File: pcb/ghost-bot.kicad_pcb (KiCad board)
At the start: 2 copper layers, 111 x 60 mm, 37 parts, among them J1 Conn_01x03_Pin, J2 Conn_01x03_Pin, J3 Conn_01x04_Pin, J4 Conn_01x02_Pin, SW1 SW_Push, SW2 SW_Push, SW3 SW_SPDT

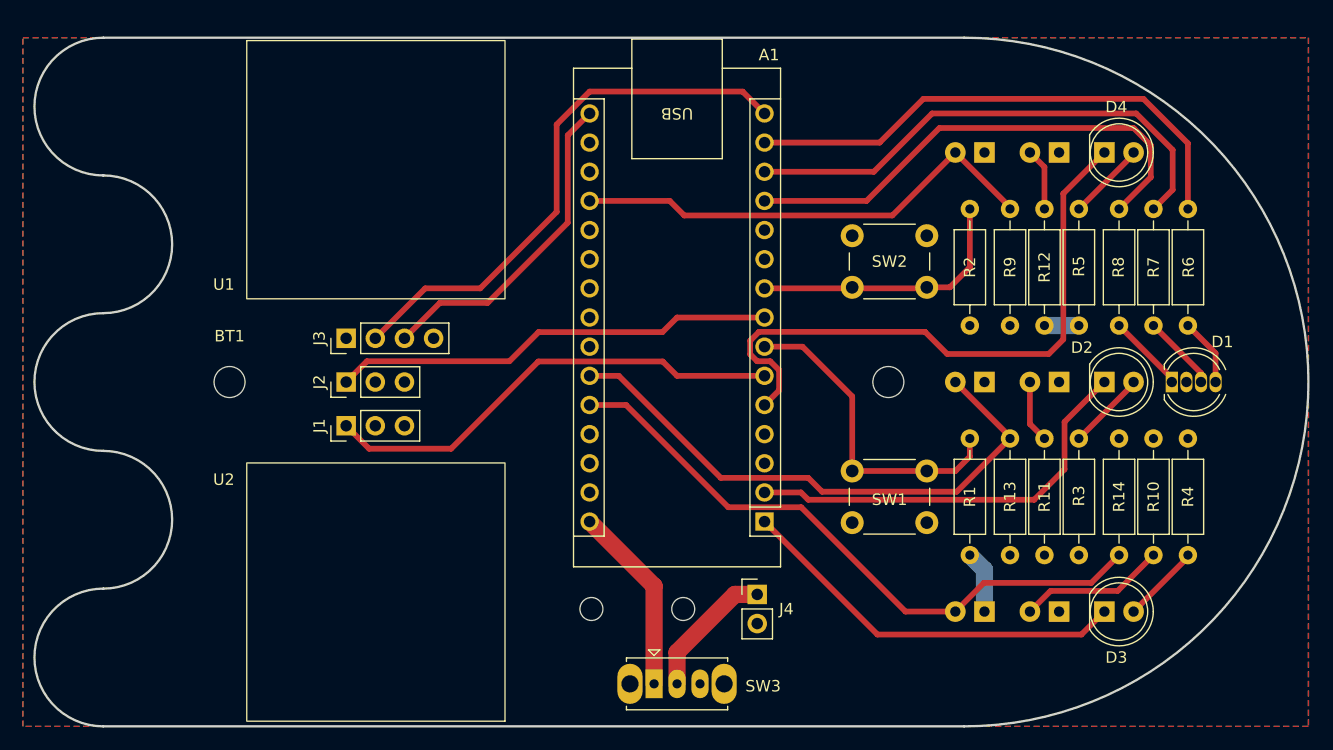
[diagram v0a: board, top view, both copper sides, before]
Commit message: Change +5V from pour to route
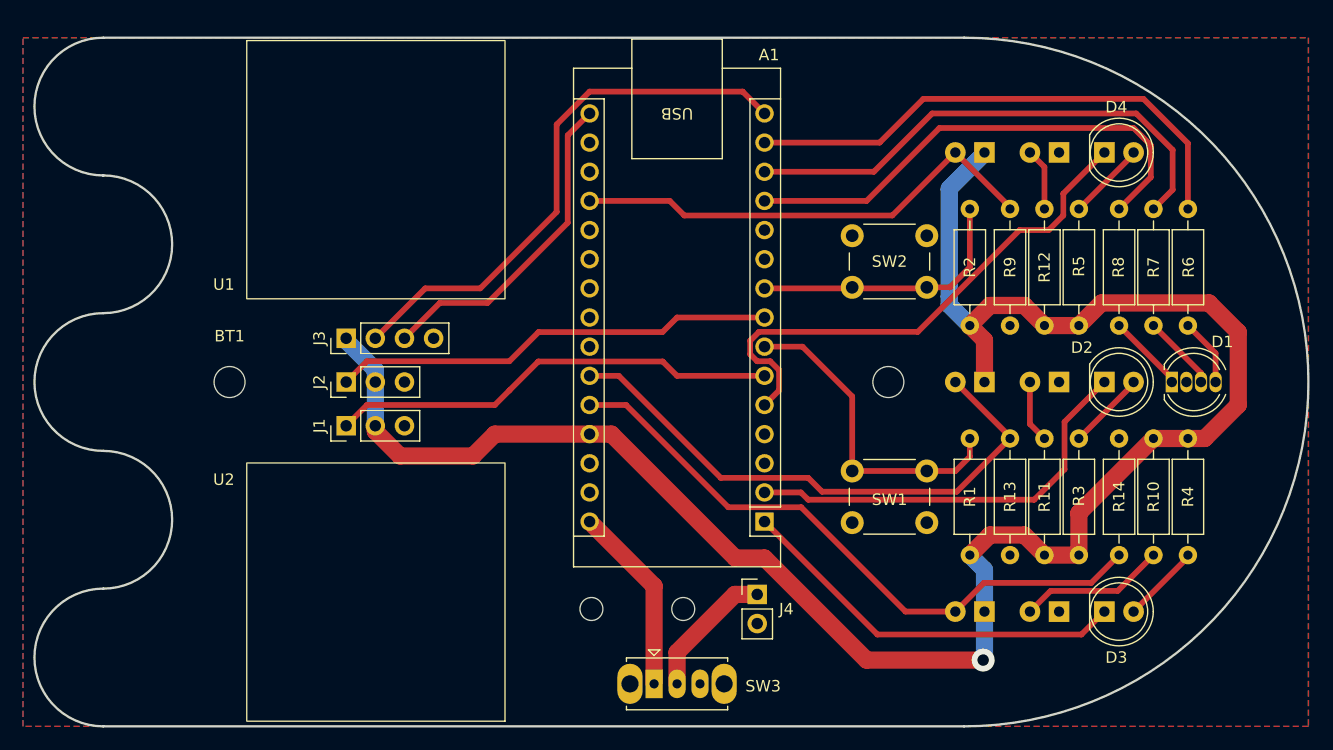
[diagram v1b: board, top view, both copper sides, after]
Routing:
- net +5V: track 8.45 -> 169.7 mm, vias 0 -> 1
- net /LED2: track 54.5 -> 46.6 mm
- net /SERVO0: track 40.9 -> 39.3 mm
- added copper zone on F.Cu, net GND
- removed copper zone on F.Cu, net +5V

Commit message: Update power switch
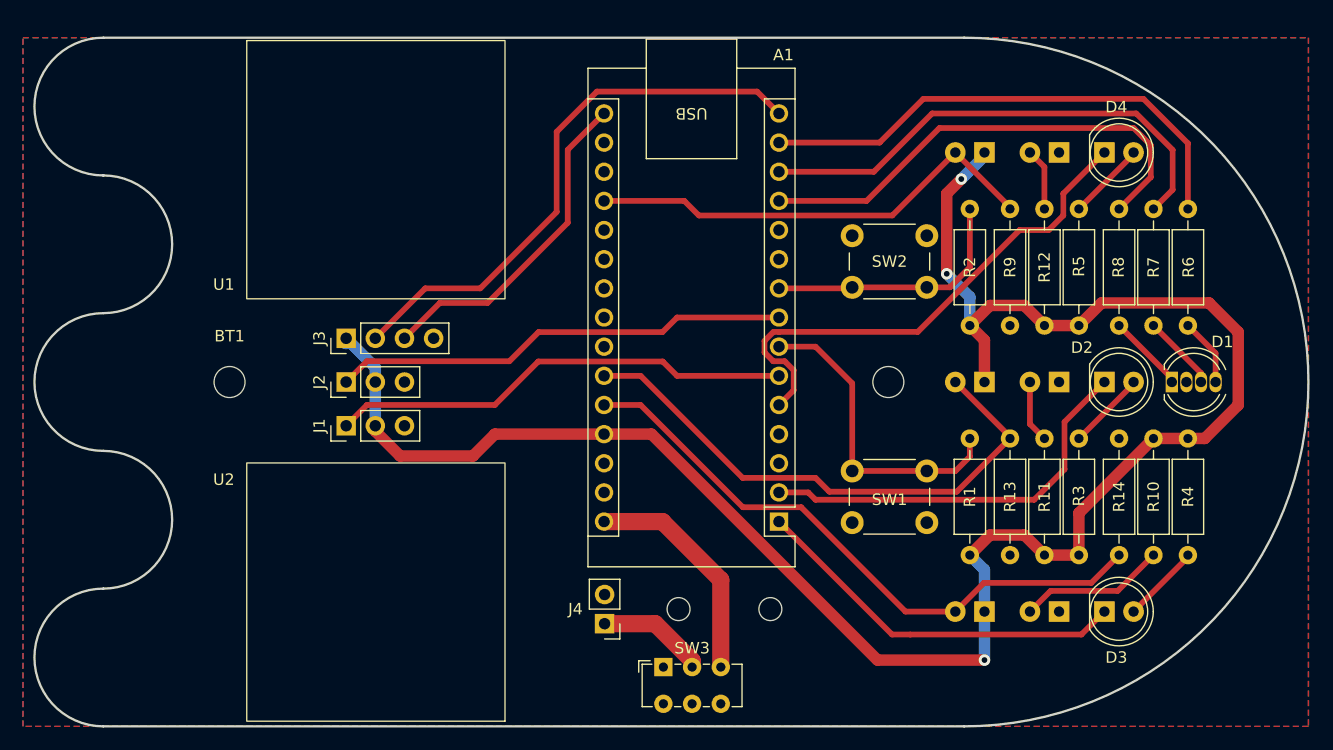
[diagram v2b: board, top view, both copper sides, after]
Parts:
- SW3: value SW_SPDT -> Switch; footprint Button_Switch_THT:SW_Slide_SPDT_Straight_CK_OS102011MS2Q -> Button_Switch_THT:SW_E-Switch_EG1271_SPDT
- moved REF** 15.6 mm to (165.6, 133.8), turned to 180 degrees
- moved J4 13.5 mm to (151.2, 135.1), turned to 180 degrees
- moved SW3 1.67 mm to (156.3, 138.8)
- moved A1 1.26 mm to (166.4, 126.2)
- moved REF** 0.41 mm to (157.6, 133.8), turned to 180 degrees
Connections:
- SW3 pad 1: +BATT_SW -> unconnected-(SW3-C-Pad1)
- SW3 pad 3: unconnected-(SW3-C-Pad3) -> +BATT_SW
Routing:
- net +BATT_SW: track 16.5 -> 19.9 mm
- net +BATT: track 11.8 -> 9.52 mm
- net /LED2: track 46.6 -> 45.3 mm
- net /LED0: track 36.5 -> 35.3 mm
- net /LED1: track 34.5 -> 33.3 mm
- net /SERVO1: track 38.8 -> 40.0 mm
- net /SERVO0: track 39.3 -> 40.5 mm
- net /RGB_R: track 45.8 -> 44.5 mm
- net /RGB_G: track 44.8 -> 43.6 mm
- net /RGB_B: track 43.6 -> 42.3 mm
- net /PD0: track 41.6 -> 40.3 mm
- net /PD2: track 55.6 -> 54.4 mm
- net /PD1: track 49.6 -> 48.4 mm
- net /PUSH_BTN1: track 23.7 -> 22.6 mm
- net /TRIG: track 48.1 -> 49.0 mm
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
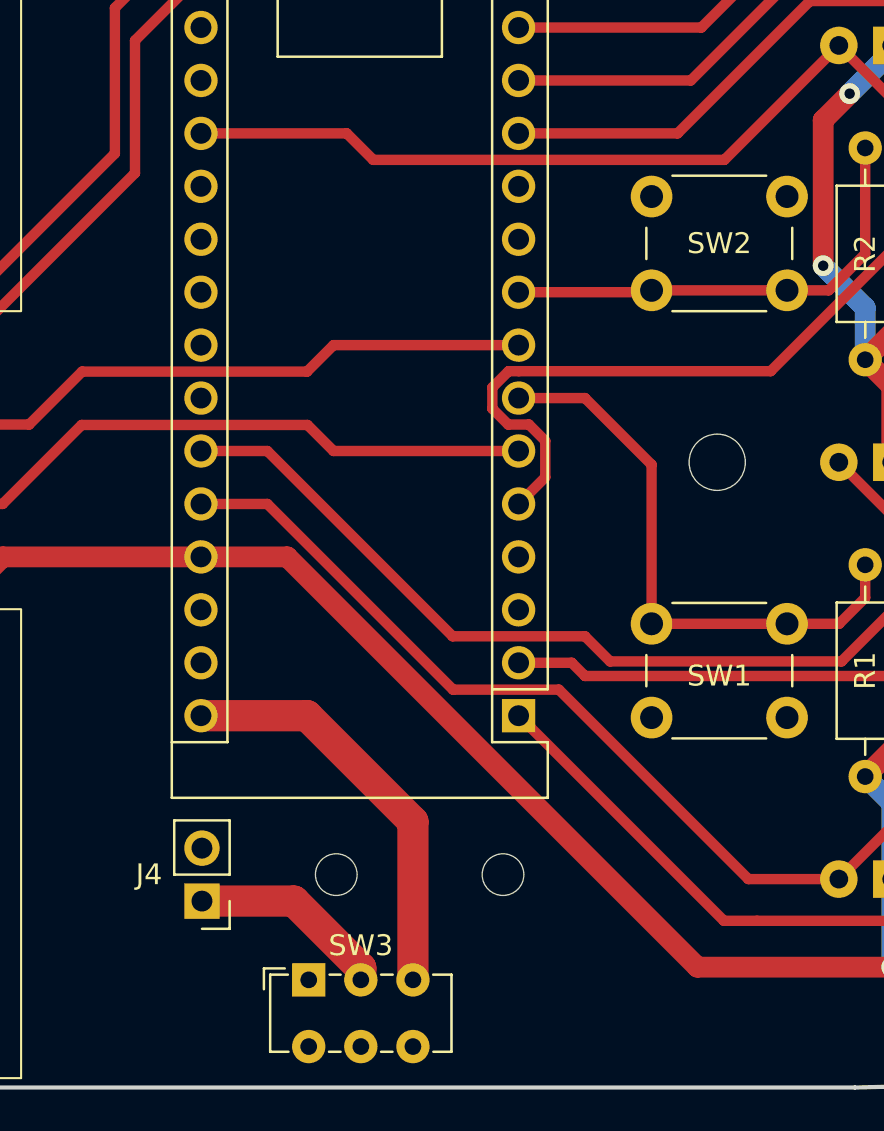
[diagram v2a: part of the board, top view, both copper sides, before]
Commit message: Add version number and blank space for name
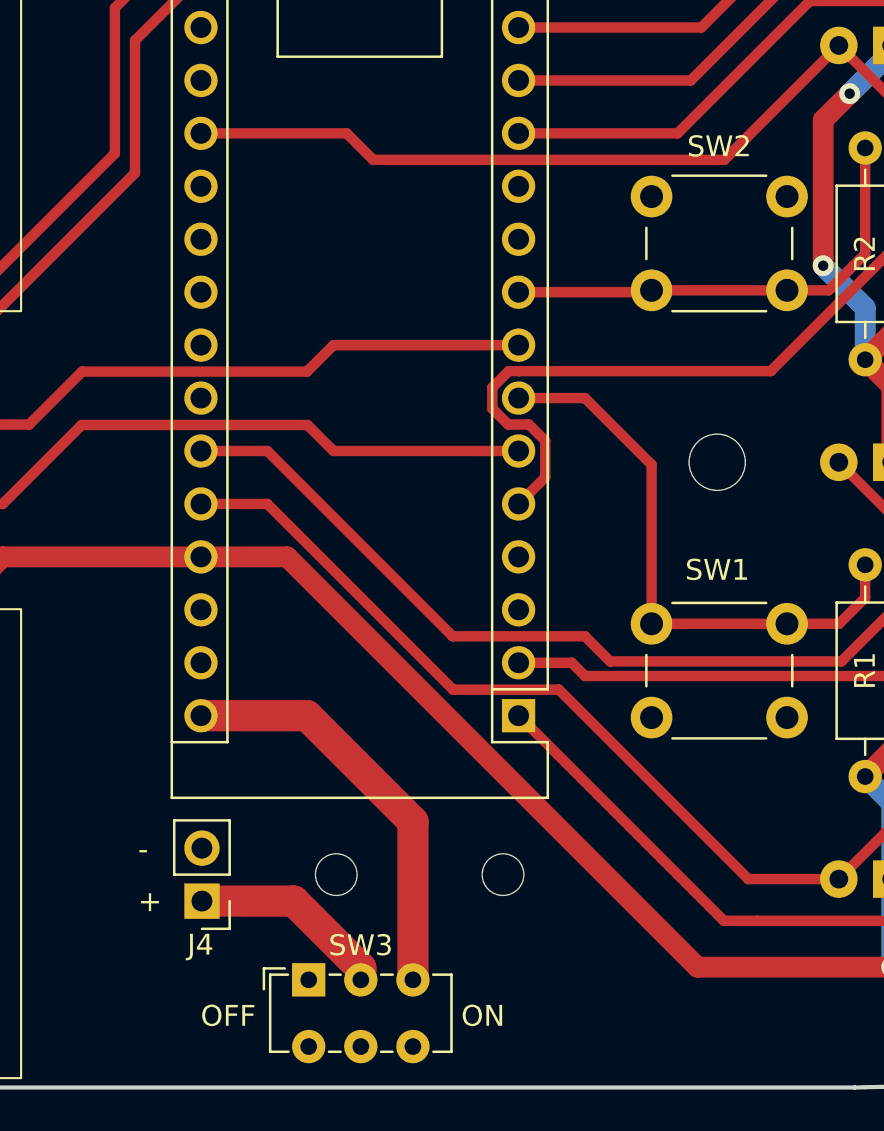
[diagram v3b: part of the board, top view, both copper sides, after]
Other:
- board text added: "+"
- board text added: "-"
- board text added: "GHOST-BOT V0.1 0424 CK"
- board text added: "OFF"
- board text added: "ON"
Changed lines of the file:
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@@
 		(pad_to_mask_clearance 0)
 		(allow_soldermask_bridges_in_footprints no)
-		(grid_origin 165.11 126.16)
+		(grid_origin 131.185 117.81)
 		(pcbplotparams
 			(layerselection 0x00010fc_ffffffff)
@@
 		(tags "Through hole pin header THT 1x02 2.54mm single row")
 		(property "Reference" "J4"
-			(at 2.54 1.275 180)
+			(at 0.067143 -2.105001 180)
 			(layer "F.SilkS")
 			(effects
@@
 		(tags "tact sw push 6mm")
 		(property "Reference" "SW1"
-			(at 3.25 2 180)
+			(at 3.345003 7.075 180)
 			(layer "F.SilkS")
 			(effects
@@
 		(tags "tact sw push 6mm")
 		(property "Reference" "SW2"
-			(at 3.25 2.25 360)
+			(at 3.25 -2.395 360)
 			(layer "F.SilkS")
 			(effects
@@
 		)
 	)
+	(gr_rect
+		(start 115.685 120.06)
+		(end 148.185 128.56)
+		(stroke
+			(width 0.1)
+			(type solid)
+		)
+		(fill solid)
+		(layer "B.SilkS")
+	)
 	(gr_line
 		(start 182.500003 144)
@@
 		(layer "Edge.Cuts")
 	)
+	(gr_text "GHOST-BOT\nV0.1 0424 CK"
+		(at 148.185 107.81 0)
+		(layer "B.SilkS" knockout)
+		(effects
+			(font
+				(size 3 3)
+				(thickness 0.3)
+			)
+			(justify left bottom mirror)
+		)
+	)
+	(gr_text "        \n        "
+		(at 140.11 141.66 0)
+		(layer "B.SilkS" knockout)
+		(effects
+			(font
+				(size 2 2)
+				(thickness 0.2)
+			)
+			(justify left bottom mirror)
+		)
+	)
+	(gr_text "OFF"
+		(at 151.11 141.16 0)
+		(layer "F.SilkS")
+		(effects
+			(font
+				(size 1 1)
+				(thickness 0.1)
+			)
+			(justify left bottom)
+		)
+	)
+	(gr_text "ON"
+		(at 163.61 141.16 0)
+		(layer "F.SilkS")
+		(effects
+			(font
+				(size 1 1)
+				(thickness 0.1)
+			)
+			(justify left bottom)
+		)
+	)
+	(gr_text "-"
+		(at 148.11 133.16 0)
+		(layer "F.SilkS")
+		(effects
+			(font
+				(size 1 1)
+				(thickness 0.1)
+			)
+			(justify left bottom)
+		)
+	)
+	(gr_text "+"
+		(at 148.11 135.66 0)
+		(layer "F.SilkS")
+		(effects
+			(font
+				(size 1 1)
+				(thickness 0.1)
+			)
+			(justify left bottom)
+		)
+	)
 	(segment
 		(start 186.500003 98.765)
@@
 		)
 	)
-	(group ""
-		(members "04ff03a6-6a82-412c-b951-cb5a4e1fd252" "235906f6-29fc-4983-abad-0b41bc71924c"
-			"b5c01504-4c51-43e4-9161-fa676d6fda77"
-		)
-	)

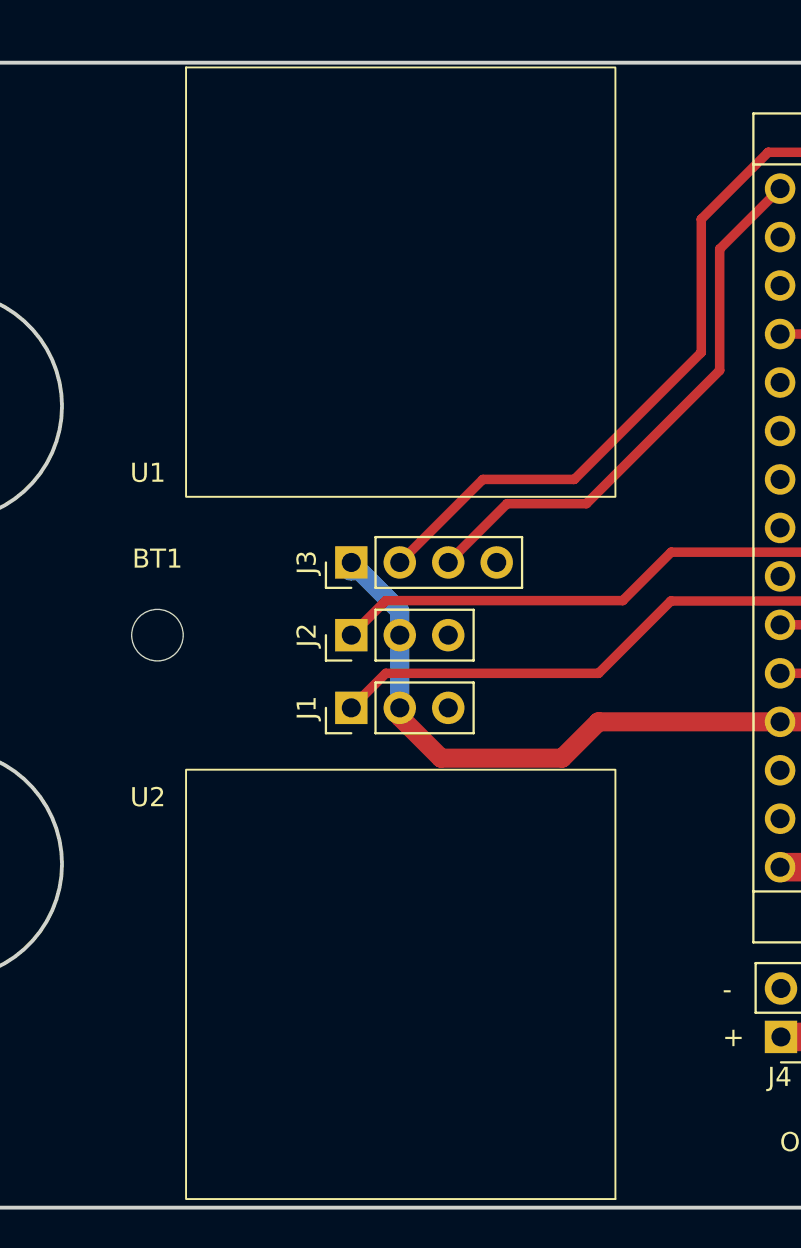
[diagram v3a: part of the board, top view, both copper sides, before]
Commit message: Fix servo 3d model, add battery holder 3d model
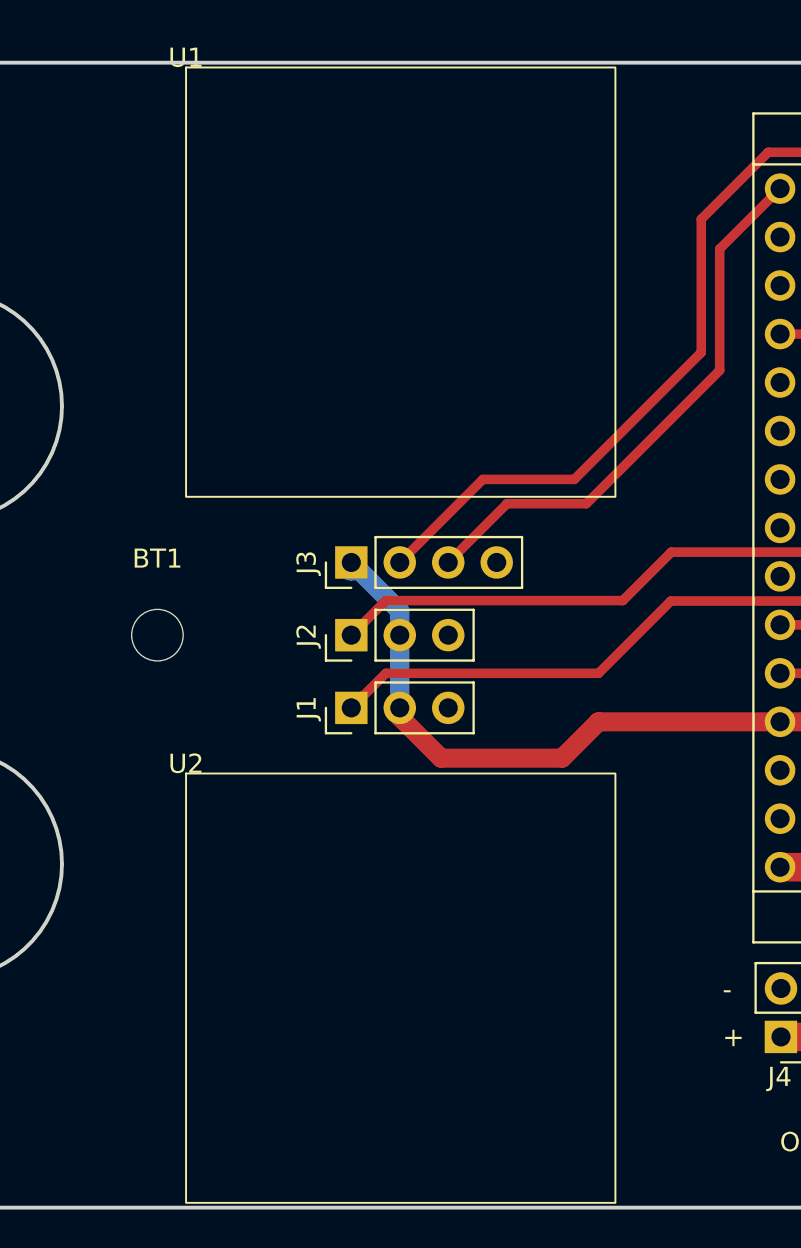
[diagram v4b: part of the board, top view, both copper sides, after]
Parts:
- U1: footprint ghost-bot-footprints:SG90 Mount -> ghost-bot-footprints:SG90 Mount Left
- U2: footprint ghost-bot-footprints:SG90 Mount -> ghost-bot-footprints:SG90 Mount Right
- moved U2 31.7 mm to (120.0, 121.2), turned to 0 degrees
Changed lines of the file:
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@@
 		)
 	)
-	(footprint "ghost-bot-footprints:SG90 Mount"
+	(footprint "ghost-bot-footprints:SG90 Mount Left"
 		(layer "F.Cu")
 		(at 120 84.25)
 		(property "Reference" "U1"
-			(at -1.999997 21.25 0)
+			(at 0 -0.5 0)
 			(unlocked yes)
 			(layer "F.SilkS")
@@
 			)
 		)
-		(property "Footprint" "ghost-bot-footprints:SG90 Mount"
+		(property "Footprint" "ghost-bot-footprints:SG90 Mount Left"
 			(at 0 0 0)
 			(unlocked yes)
@@
 			)
 		)
-		(sheetname "Root")
-		(sheetfile "ghost-bot.kicad_sch")
 		(attr through_hole)
 		(fp_circle
@@
 		)
 		(group ""
-			(members "477627c3-0ea7-40b4-8d42-3f0d67e40fb8" "54bcdb0e-7c43-4856-8c80-bbe86b502977"
-				"5983bcc4-ed36-4caf-9558-bb0dae69b7ae" "8df0314b-b93d-4c92-ba53-34634ea4101a"
-				"ac0160a3-3629-4786-8965-1265075b70f3" "bec5e667-489f-4c43-b3b2-1797f995ca7c"
-				"d24b03ea-7639-4392-9dd7-51629ad52e89" "d7f80189-96fb-43f1-8ea7-0dccd5c6819d"
-				"db8f25e3-8522-4877-baae-065b9b1cb244" "ef4a4cf2-f2c1-4e7a-9d7d-72907f004f8e"
+			(members "065eebc5-e58f-4e5b-9ba1-1c761c134878" "2c3f43af-45b5-4842-b803-4c5029c35410"
+				"3bd75768-710e-4287-b6c3-907f92769104" "56f2f07b-8d62-44bc-bd64-2dcf287d6864"
+				"701e2a11-0f14-494c-988a-4f912dfa61e6" "aa18958b-b5a4-417a-be25-1ae46ee51011"
+				"ca628f01-edbf-4ea8-ad5c-528ef7bb0ef0" "dc04df5b-5c4c-423c-94cf-c9e431fd34a8"
+				"e07d17e8-bc87-48b7-bbab-782ed894ede9" "e5fc3e63-8c5c-41db-b08d-42a8e39c4b29"
 			)
 		)
 		(group ""
-			(members "89dbb5f2-834d-4435-8ff6-2a0a1a8e5e7e" "8ea8d284-649a-4601-8775-b0ddb1f1a850"
-				"c0ae5fb2-2f40-476a-8581-44509fb10b3a"
+			(members "42162b86-009d-4845-8768-e036fcf516e4" "813d3f72-5694-440b-8c18-e3150fbfc66d"
+				"d4edf60a-675a-45d9-8a4b-d10af0728610"
+			)
+		)
+		(model "C:/CAD/2478CN/2478 with standoffs.step"
+			(offset
+				(xyz 28 0.5 27.5)
+			)
+			(scale
+				(xyz 1 1 1)
+			)
+			(rotate
+				(xyz -90 0 90)
 			)
 		)
@@
 		)
 	)
-	(footprint "ghost-bot-footprints:SG90 Mount"
+	(footprint "ghost-bot-footprints:SG90 Mount Right"
 		(layer "F.Cu")
-		(at 142.5 143.55 180)
+		(at 120 121.25)
 		(property "Reference" "U2"
-			(at 24.499997 21.05 0)
+			(at 0 -0.5 0)
 			(unlocked yes)
 			(layer "F.SilkS")
@@
 		)
 		(property "Value" "~"
-			(at 0 1 180)
+			(at 0 1 0)
 			(unlocked yes)
 			(layer "F.Fab")
@@
 			)
 		)
-		(property "Footprint" "ghost-bot-footprints:SG90 Mount"
-			(at 0 0 180)
+		(property "Footprint" "ghost-bot-footprints:SG90 Mount Right"
+			(at 0 0 0)
 			(unlocked yes)
 			(layer "F.Fab")
@@
 		)
 		(property "Datasheet" ""
-			(at 0 0 180)
+			(at 0 0 0)
 			(unlocked yes)
 			(layer "F.Fab")
@@
 		)
 		(property "Description" ""
-			(at 0 0 180)
+			(at 0 0 0)
 			(unlocked yes)
 			(layer "F.Fab")
@@
 		)
 		(fp_text user "${REFERENCE}"
-			(at 0 2.5 180)
+			(at 0 2.5 0)
 			(unlocked yes)
 			(layer "F.Fab")
@@
 		)
 		(pad "" np_thru_hole oval
-			(at -2.5 11.25 180)
+			(at -2.5 11.25)
 			(size 2.5 5)
 			(drill oval 2.5 5)
@@
 		)
 		(pad "" np_thru_hole oval
-			(at 25 11.25 180)
+			(at 25 11.25)
 			(size 2.5 5)
 			(drill oval 2.5 5)
@@
 			(polygon
 				(pts
-					(xy 146.5 143.55) (xy 116 143.55) (xy 116 121.05) (xy 146.5 121.05)
+					(xy 116 121.25) (xy 146.5 121.25) (xy 146.5 143.75) (xy 116 143.75)
 				)
 			)
@@
 		(model "C:/CAD/sg90-micro-servo-9g-tower-pro-1.snapshot.3/SG90 - Micro Servo 9g - Tower Pro.STEP"
 			(offset
-				(xyz 4.5 -28.5 -21.75)
+				(xyz 4.5 6.5 33.75)
 			)
 			(scale
@@
 			)
 			(rotate
-				(xyz 0 0 0)
+				(xyz 180 0 0)
 			)
 		)
@@
 		(min_thickness 0.25)
 		(filled_areas_thickness no)
-		(fill yes
+		(fill
 			(thermal_gap 0.5)
 			(thermal_bridge_width 0.5)
@@
 		(min_thickness 0.25)
 		(filled_areas_thickness no)
-		(fill yes
+		(fill
 			(thermal_gap 0.5)
 			(thermal_bridge_width 0.5)
